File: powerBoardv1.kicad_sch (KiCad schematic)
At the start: 29 parts, among them J2 USB_C_Receptacle_USB2.0_14P, Q1 PNP, U1 LMR62014XMF

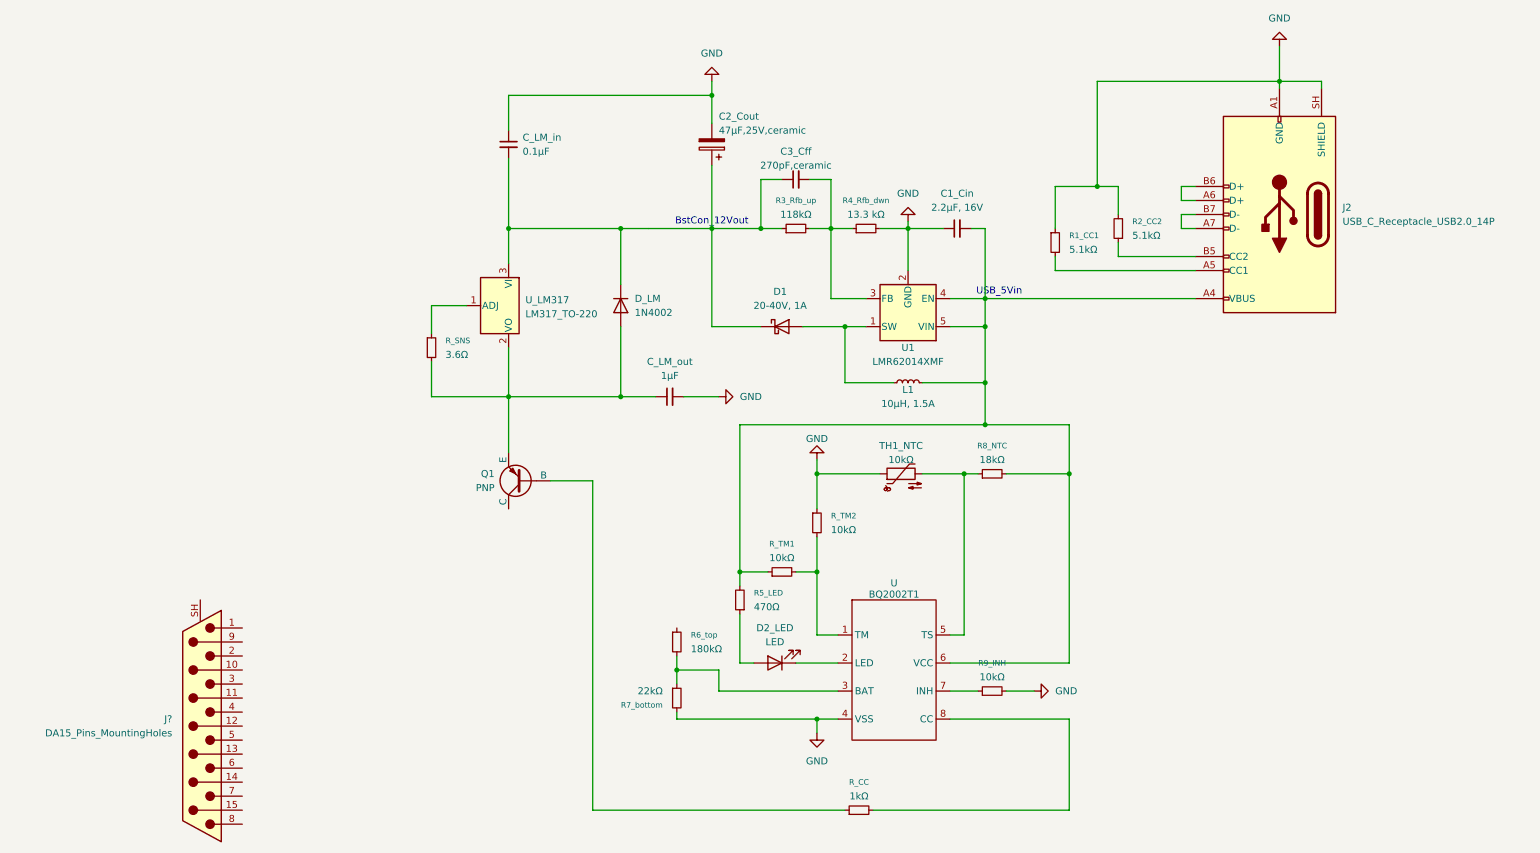
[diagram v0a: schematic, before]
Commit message: network is complete, all pins are connected
but footprint of all the components & subcomponents are not yet assigned or validated.
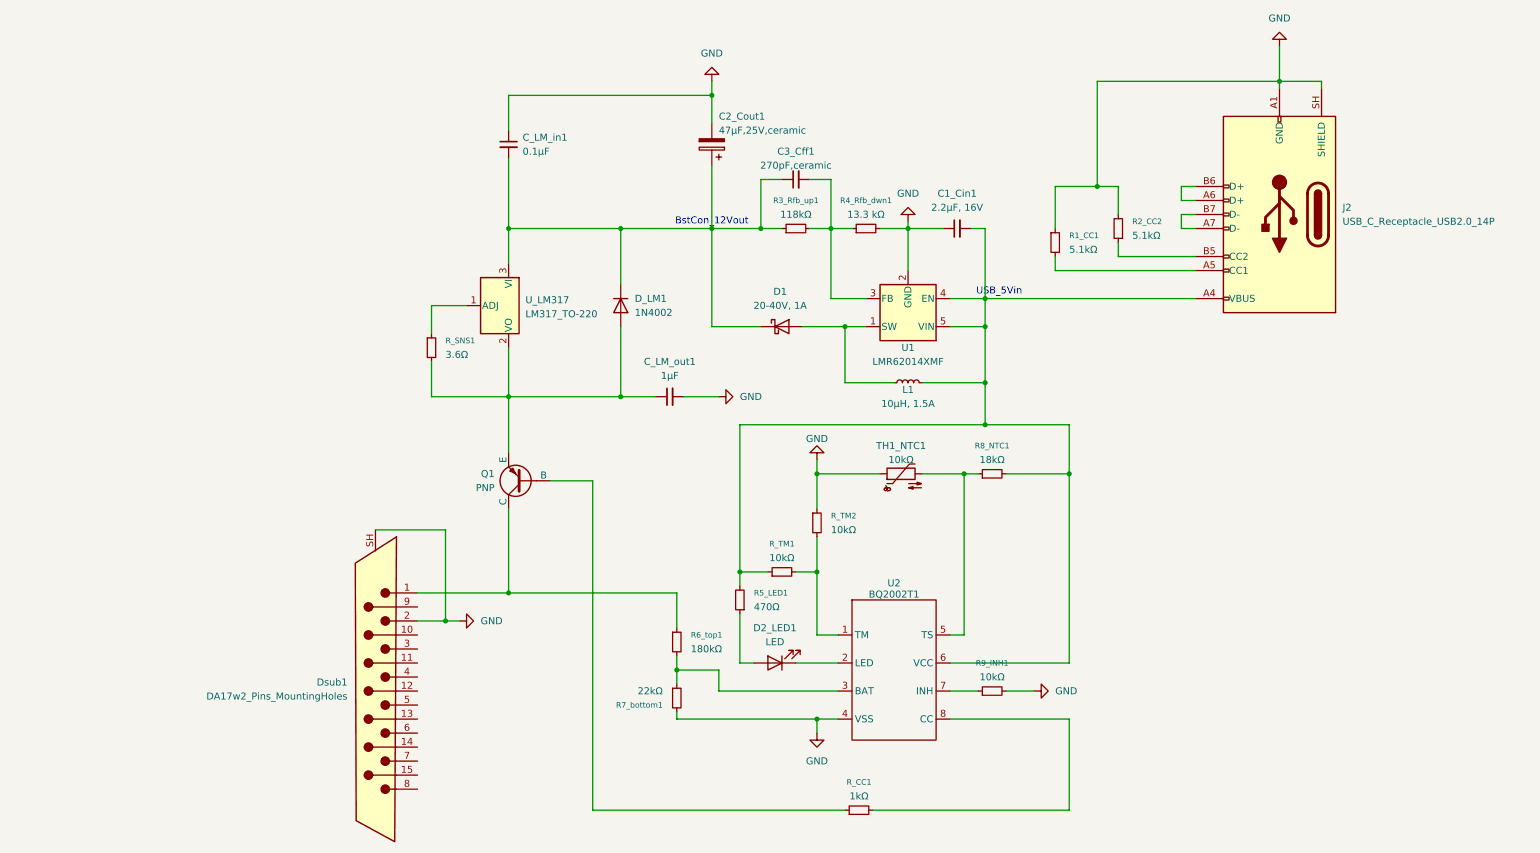
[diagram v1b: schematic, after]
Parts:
- removed J?: DA15_Pins_MountingHoles, symbol Connector:DA15_Pins_MountingHoles
- added Dsub1: DA17w2_Pins_MountingHoles, CONN_FM17W2P1-K120_MOL, symbol powerBoardCustomLibrary:DA17w2_Pins_MountingHoles
- J2: footprint (none) -> Connector_USB:USB_C_Receptacle_GCT_USB4105-xx-A_16P_TopMnt_Horizontal
- U1: footprint Package_TO_SOT_SMD:SOT-23-5 -> Package_TO_SOT_SMD:SOT-23-5_HandSoldering
- renumbered C1_Cin to C1_Cin1, C2_Cout to C2_Cout1, C3_Cff to C3_Cff1, C_LM_in to C_LM_in1, C_LM_out to C_LM_out1, D2_LED to D2_LED1, D_LM to D_LM1, R3_Rfb_up to R3_Rfb_up1, R4_Rfb_dwn to R4_Rfb_dwn1, R5_LED to R5_LED1, R6_top to R6_top1, R7_bottom to R7_bottom1, R8_NTC to R8_NTC1, R9_INH to R9_INH1, R_CC to R_CC1, R_SNS to R_SNS1, TH1_NTC to TH1_NTC1, U to U2
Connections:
- net GND: now also Dsub1.2, Dsub1.SH (PAD)
- net at Q1.1 (C): now also R6_top1.1, Dsub1.1

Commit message: footprints assigned
this iteration has footprints assigned. Dsub-17w2's footprint for kicad v6 is downloaded from digikey, used and also uploaded in the repo
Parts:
- C1_Cin1: footprint (none) -> Capacitor_SMD:C_1206_3216Metric_Pad1.33x1.80mm_HandSolder
- C2_Cout1: footprint (none) -> Capacitor_SMD:C_1210_3225Metric_Pad1.33x2.70mm_HandSolder
- C3_Cff1, C_LM_in1, C_LM_out1: footprint (none) -> Capacitor_SMD:C_0805_2012Metric_Pad1.18x1.45mm_HandSolder
- D1: footprint (none) -> Diode_THT:D_DO-41_SOD81_P10.16mm_Horizontal
- D2_LED1: footprint (none) -> LED_THT:LED_D5.0mm
- L1: footprint (none) -> Inductor_THT:L_Axial_L9.5mm_D4.0mm_P15.24mm_Horizontal_Fastron_SMCC
- Q1_PNP1: renamed from Q1; value PNP -> 2N3906; footprint (none) -> Package_TO_SOT_THT:TO-92_Inline
- R1_CC1, R2_CC2, R3_Rfb_up1, R4_Rfb_dwn1, R5_LED1, R6_top1, R7_bottom1, R8_NTC1, R9_INH1, R_CC1, R_SNS1, R_TM1, R_TM2, TH1_NTC1: footprint (none) -> Resistor_THT:R_Axial_DIN0207_L6.3mm_D2.5mm_P10.16mm_Horizontal
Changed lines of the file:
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@@
 			)
 		)
-		(property "Footprint" ""
+		(property "Footprint" "Resistor_THT:R_Axial_DIN0207_L6.3mm_D2.5mm_P10.16mm_Horizontal"
 			(at 158.75 107.95 0)
 			(hide yes)
@@
 			)
 		)
-		(property "Footprint" ""
+		(property "Footprint" "Resistor_THT:R_Axial_DIN0207_L6.3mm_D2.5mm_P10.16mm_Horizontal"
 			(at 133.35 139.7 0)
 			(hide yes)
@@
 			)
 		)
-		(property "Footprint" ""
+		(property "Footprint" "Capacitor_SMD:C_1210_3225Metric_Pad1.33x2.70mm_HandSolder"
 			(at 138.7348 35.56 0)
 			(hide yes)
@@
 			)
 		)
-		(property "Footprint" ""
+		(property "Footprint" "Diode_THT:D_DO-41_SOD81_P10.16mm_Horizontal"
 			(at 152.4 72.39 0)
 			(hide yes)
@@
 			)
 		)
-		(property "Footprint" ""
+		(property "Footprint" "Resistor_THT:R_Axial_DIN0207_L6.3mm_D2.5mm_P10.16mm_Horizontal"
 			(at 154.94 54.61 0)
 			(hide yes)
@@
 			)
 		)
-		(property "Footprint" ""
+		(property "Footprint" "Resistor_THT:R_Axial_DIN0207_L6.3mm_D2.5mm_P10.16mm_Horizontal"
 			(at 190.5 138.43 0)
 			(hide yes)
@@
 			)
 		)
-		(property "Footprint" ""
+		(property "Footprint" "Capacitor_SMD:C_0805_2012Metric_Pad1.18x1.45mm_HandSolder"
 			(at 154.94 45.72 0)
 			(hide yes)
@@
 			)
 		)
-		(property "Footprint" ""
+		(property "Footprint" "Capacitor_SMD:C_1206_3216Metric_Pad1.33x1.80mm_HandSolder"
 			(at 184.15 54.61 0)
 			(hide yes)
@@
 			)
 		)
-		(property "Footprint" ""
+		(property "Footprint" "Resistor_THT:R_Axial_DIN0207_L6.3mm_D2.5mm_P10.16mm_Horizontal"
 			(at 144.78 121.92 0)
 			(hide yes)
@@
 			)
 		)
-		(property "Footprint" ""
+		(property "Footprint" "Resistor_THT:R_Axial_DIN0207_L6.3mm_D2.5mm_P10.16mm_Horizontal"
 			(at 190.5 99.06 0)
 			(hide yes)
@@
 		(dnp no)
 		(fields_autoplaced yes)
-		(property "Reference" "Q1"
+		(property "Reference" "Q1_PNP1"
 			(at 100.33 99.0599 0)
 			(show_name no)
@@
 			)
 		)
-		(property "Value" "PNP"
+		(property "Value" "2N3906"
 			(at 100.33 101.5999 0)
 			(show_name no)
@@
 			)
 		)
-		(property "Footprint" ""
+		(property "Footprint" "Package_TO_SOT_THT:TO-92_Inline"
 			(at 69.85 100.33 0)
 			(hide yes)
@@
 			(project "powerBoardv1"
 				(path "/e61e13dc-3a56-4575-99e0-403c3d100eff"
-					(reference "Q1")
+					(reference "Q1_PNP1")
 					(unit 1)
 				)
@@
 			)
 		)
-		(property "Footprint" ""
+		(property "Footprint" "Resistor_THT:R_Axial_DIN0207_L6.3mm_D2.5mm_P10.16mm_Horizontal"
 			(at 133.35 129.54 0)
 			(hide yes)
@@
 			)
 		)
-		(property "Footprint" ""
+		(property "Footprint" "Resistor_THT:R_Axial_DIN0207_L6.3mm_D2.5mm_P10.16mm_Horizontal"
 			(at 152.4 116.84 0)
 			(hide yes)
@@
 			)
 		)
-		(property "Footprint" ""
+		(property "Footprint" "Inductor_THT:L_Axial_L9.5mm_D4.0mm_P15.24mm_Horizontal_Fastron_SMCC"
 			(at 175.26 82.55 0)
 			(hide yes)
@@
 			)
 		)
-		(property "Footprint" ""
+		(property "Footprint" "Resistor_THT:R_Axial_DIN0207_L6.3mm_D2.5mm_P10.16mm_Horizontal"
 			(at 172.72 99.06 0)
 			(hide yes)
@@
 			)
 		)
-		(property "Footprint" ""
+		(property "Footprint" "Resistor_THT:R_Axial_DIN0207_L6.3mm_D2.5mm_P10.16mm_Horizontal"
 			(at 213.36 54.61 0)
 			(hide yes)
@@
 			)
 		)
-		(property "Footprint" ""
+		(property "Footprint" "Capacitor_SMD:C_0805_2012Metric_Pad1.18x1.45mm_HandSolder"
 			(at 102.87 39.37 0)
 			(hide yes)
@@
 			)
 		)
-		(property "Footprint" ""
+		(property "Footprint" "Resistor_THT:R_Axial_DIN0207_L6.3mm_D2.5mm_P10.16mm_Horizontal"
 			(at 88.9 76.2 0)
 			(hide yes)
@@
 			)
 		)
-		(property "Footprint" ""
+		(property "Footprint" "LED_THT:LED_D5.0mm"
 			(at 151.13 133.35 0)
 			(hide yes)
@@
 			)
 		)
-		(property "Footprint" ""
+		(property "Footprint" "Resistor_THT:R_Axial_DIN0207_L6.3mm_D2.5mm_P10.16mm_Horizontal"
 			(at 167.64 54.61 0)
 			(hide yes)
@@
 			)
 		)
-		(property "Footprint" ""
+		(property "Footprint" "Resistor_THT:R_Axial_DIN0207_L6.3mm_D2.5mm_P10.16mm_Horizontal"
 			(at 201.93 57.15 0)
 			(hide yes)
@@
 			)
 		)
-		(property "Footprint" ""
+		(property "Footprint" "Resistor_THT:R_Axial_DIN0207_L6.3mm_D2.5mm_P10.16mm_Horizontal"
 			(at 166.37 160.02 0)
 			(hide yes)
@@
 			)
 		)
-		(property "Footprint" ""
+		(property "Footprint" "Capacitor_SMD:C_0805_2012Metric_Pad1.18x1.45mm_HandSolder"
 			(at 132.08 85.09 0)
 			(hide yes)

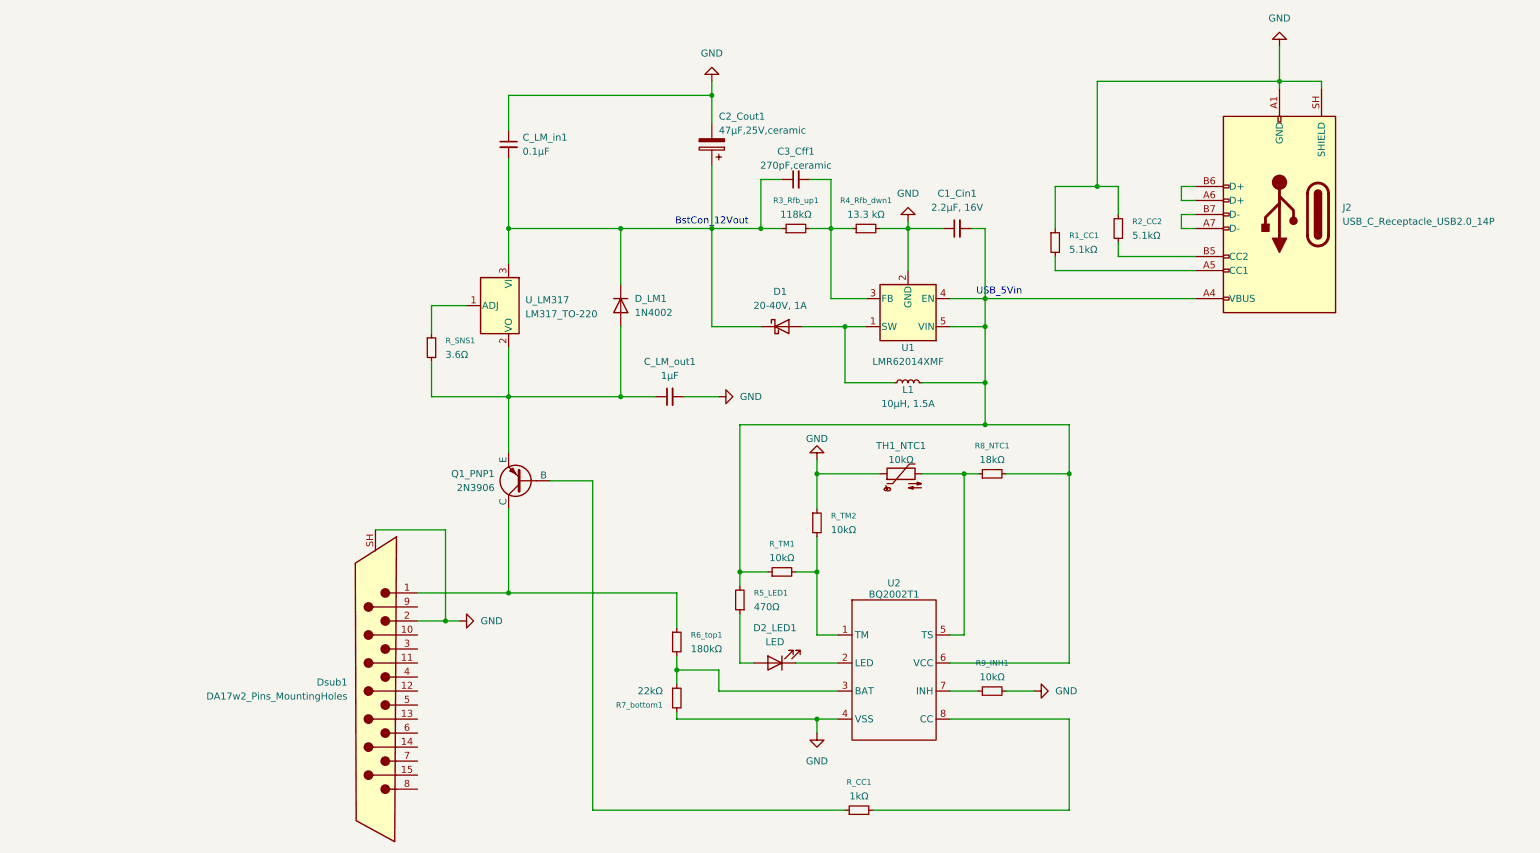
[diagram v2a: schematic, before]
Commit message: the '_sch' file contains Francesco's revisions
Mr Franscesco's revision regarding: 
1. the positioning of the NTC being on the battery instead of the PCB. 
2. the change in R_CC. This R_CC is connected to the node of BQ2002T pin CC. To lower the current coming into this pin from the PNP
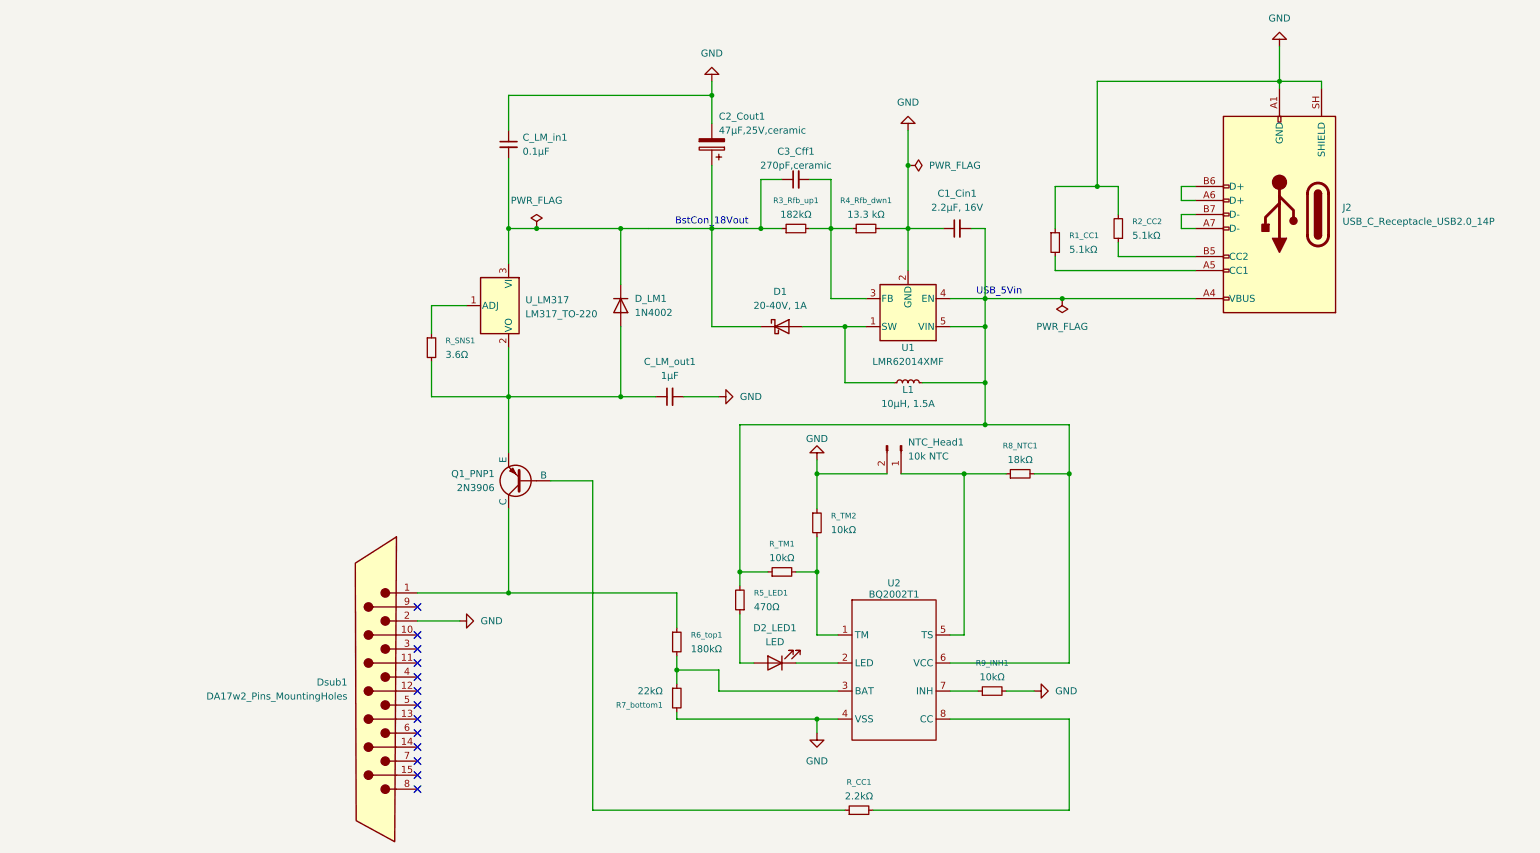
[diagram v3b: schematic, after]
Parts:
- removed TH1_NTC1: 10kΩ, Resistor_THT:R_Axial_DIN0207_L6.3mm_D2.5mm_P10.16mm_Horizontal, symbol Device:Thermistor_NTC
- added NTC_Head1: 10k NTC, Connector_PinHeader_2.54mm:PinHeader_1x02_P2.54mm_Vertical, symbol Connector:Conn_01x02_Pin
- R3_Rfb_up1: value 118kΩ -> 182kΩ
- R_CC1: value 1kΩ -> 2.2kΩ
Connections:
- net GND: now also NTC_Head1.2 (Pin_2); no longer Dsub1.SH (PAD)
- net at R8_NTC1.1, U2.5 (TS): now also NTC_Head1.1 (Pin_1)
- no-connect marks 0 -> 13
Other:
- note added: "BstCon_18Vout"
- note removed: "BstCon_12Vout"
- moved on the sheet: R8_NTC1
